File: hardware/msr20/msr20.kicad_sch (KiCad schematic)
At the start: 0 parts

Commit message: add cd74hc4046 symbol
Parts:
- added C1: 200n, symbol Device:C
- added C2: 2.2u, symbol Device:C
- added C3: 1.5p, symbol Device:C
- added L1: 5.1n, symbol Device:L
- added L2: 15u, symbol Device:L
- added R1: 1.5k, symbol Device:R
- added U1: RF-BPF, symbol msr20:RF-BPF
- added U2: BGA616, symbol msr20:BGA616
- added U3: ADE-1+, symbol msr20:ADE-1+
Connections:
- new net: C2.1, L1.2, R1.2, U2.3 (OUT)
- new net: C2.2, U3.3 (RF)
- new net: C1.1, L2.2, U2.1 (IN)
- new net: C1.2, R1.1
- new net: C3.1, L2.1, U1.7 (OUT), U1.8 (OUT)
- new net +3.3V: L1.1
- new net GND: C3.2, U1.3 (GND), U1.4 (GND), U1.5 (GND), U1.6 (GND), U2.2 (GND), U2.4 (GND), U3.1 (GND), U3.4 (GND), U3.5 (GND)
- new net RF-IN: U1.1 (IN), U1.2 (IN)

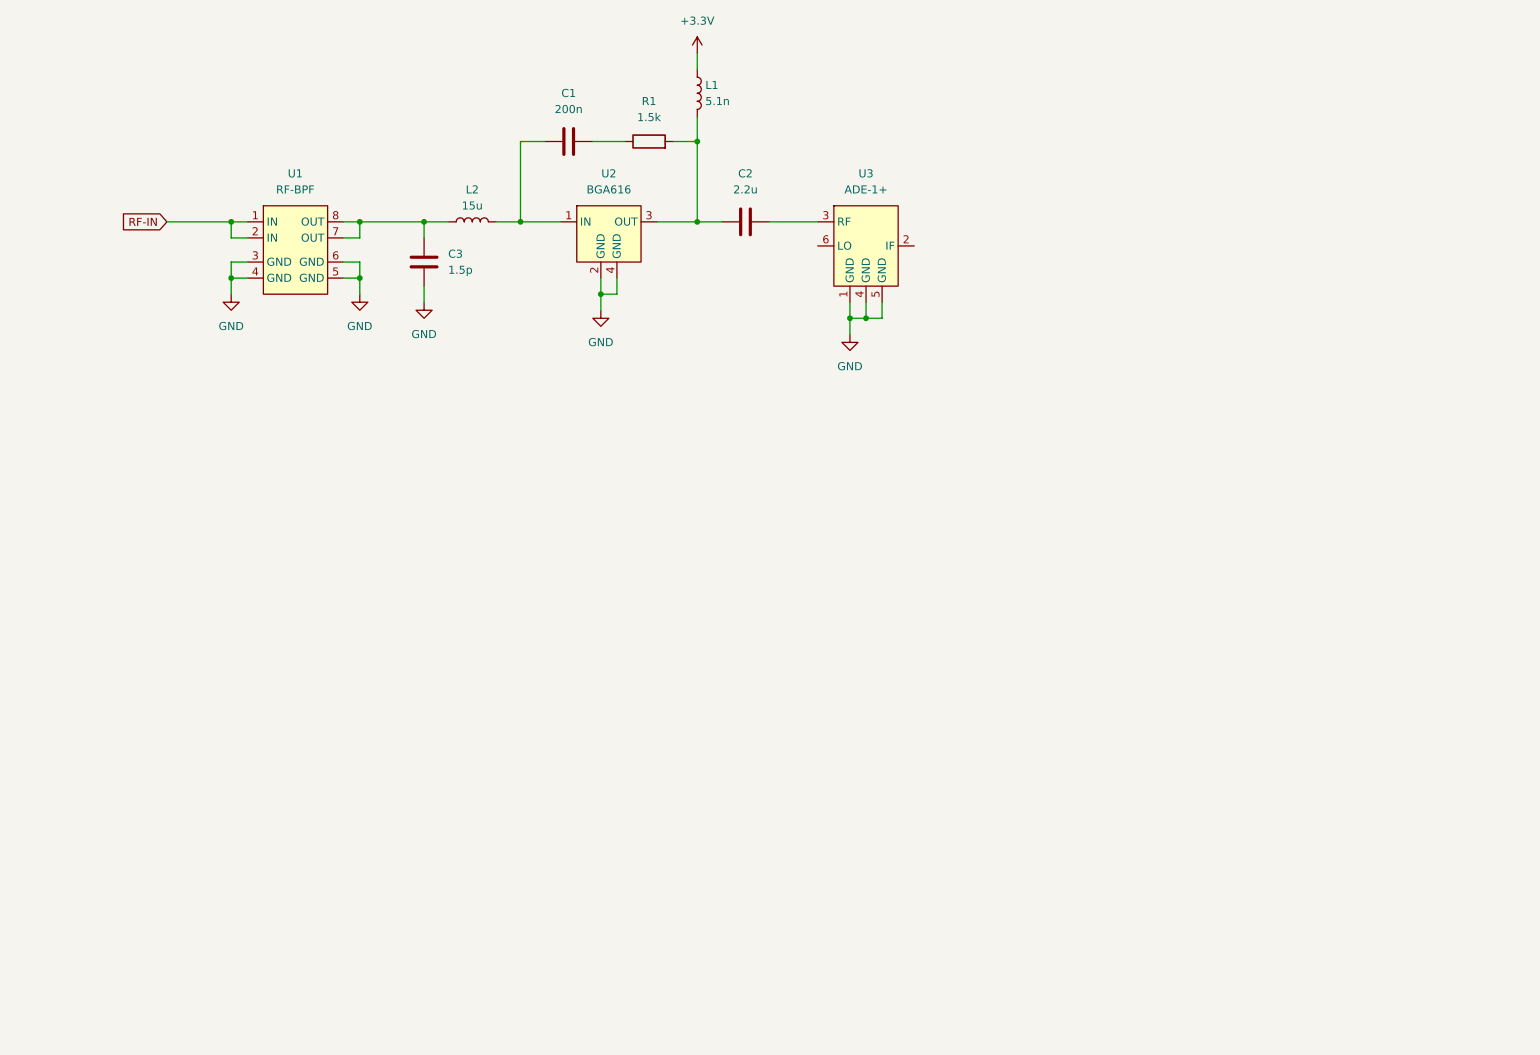
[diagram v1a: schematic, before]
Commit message: add adc and pico to sch
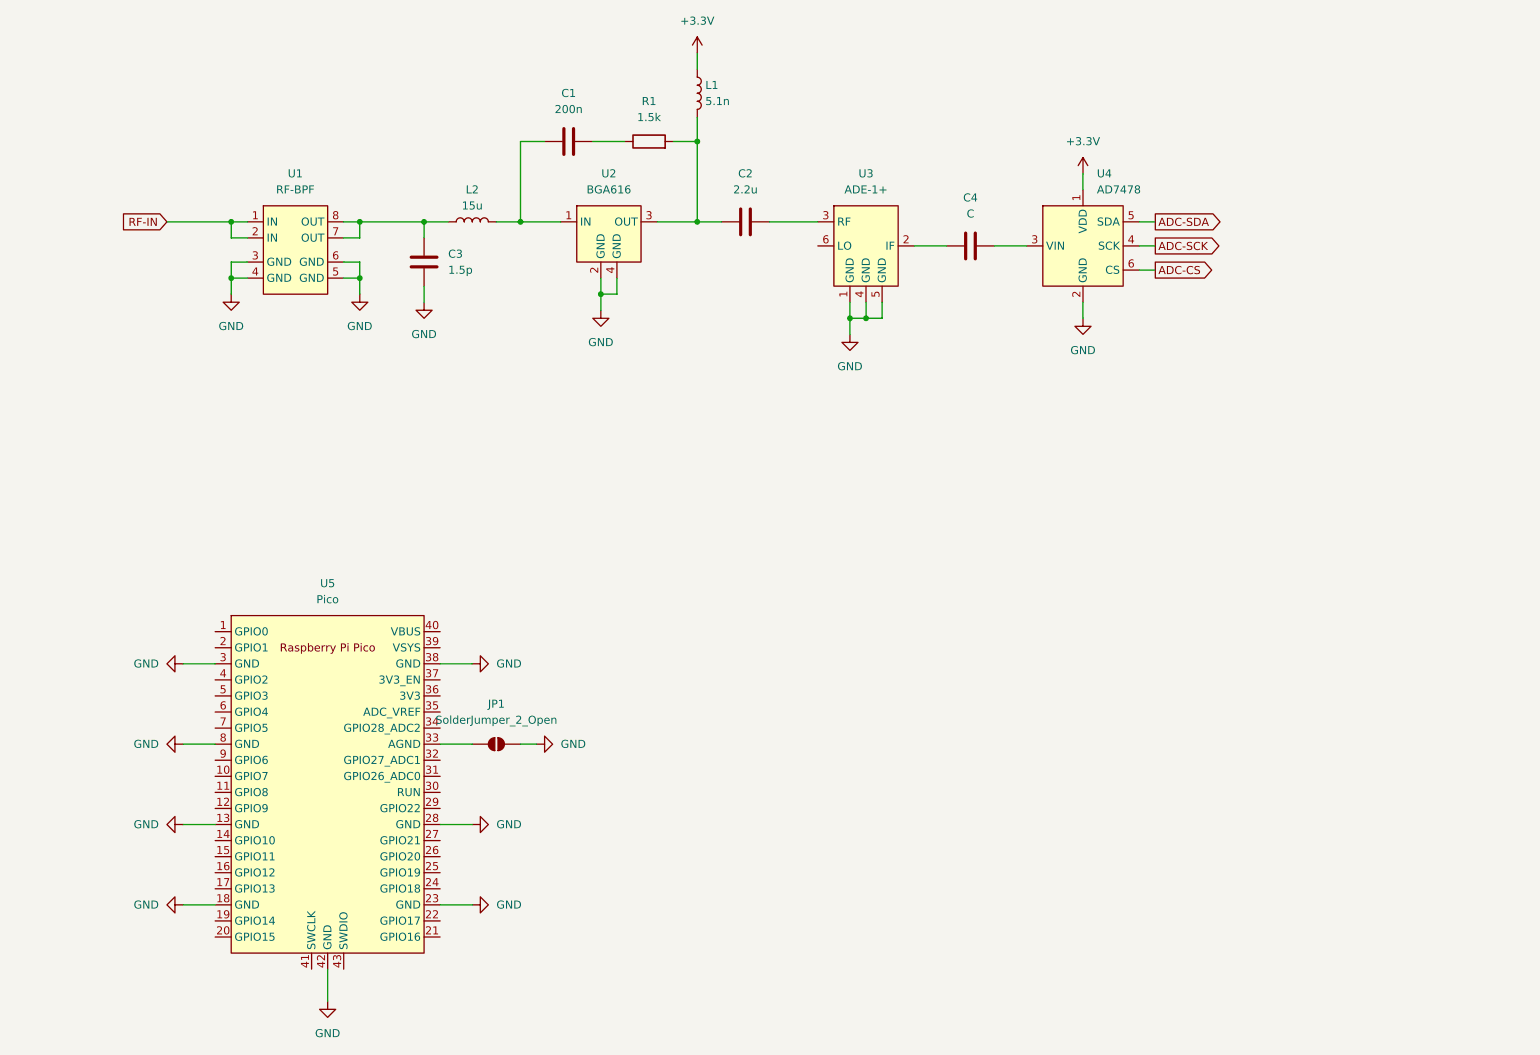
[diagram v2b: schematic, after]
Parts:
- added C4: C, symbol Device:C
- added JP1: SolderJumper_2_Open, symbol Jumper:SolderJumper_2_Open
- added U4: AD7478, symbol msr20:AD7478
- added U5: Pico, RPi_Pico:RPi_Pico_SMD_TH, symbol MCU_RaspberryPi_and_Boards:Pico
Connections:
- net +3.3V: now also U4.1 (VDD)
- net GND: now also JP1.2 (B), U4.2 (GND), U5.13 (GND), U5.18 (GND), U5.23 (GND), U5.28 (GND), U5.3 (GND), U5.38 (GND), U5.42 (GND), U5.8 (GND)
- net at U3.2 (IF): now also C4.1
- new net: JP1.1 (A), U5.33 (AGND)
- new net: C4.2, U4.3 (VIN)
- new net ADC-CS: U4.6 (CS)
- new net ADC-SCK: U4.4 (SCK)
- new net ADC-SDA: U4.5 (SDA)

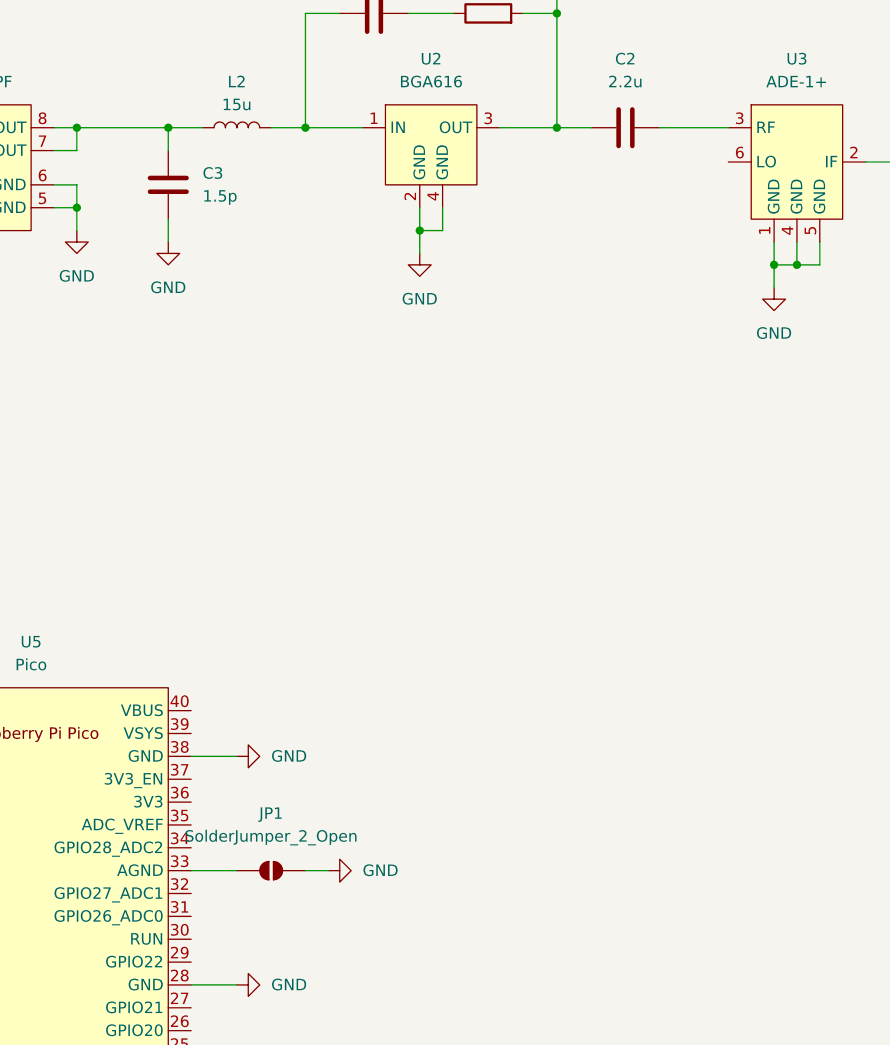
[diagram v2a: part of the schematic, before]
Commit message: Add pll schematic
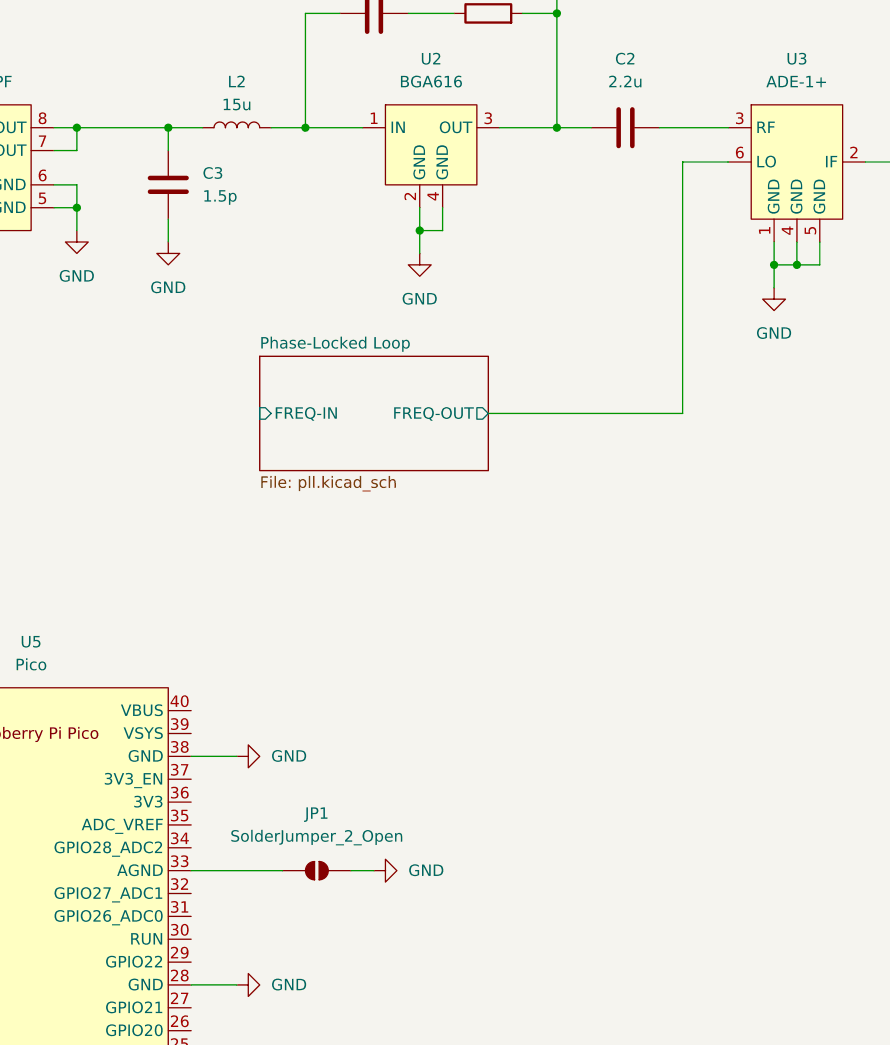
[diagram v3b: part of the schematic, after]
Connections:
- net Phase-Locked Loop/FREQ-OUT: now reaches U3.6 (LO)
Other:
- added sheet Phase-Locked Loop (pll.kicad_sch)
- moved on the sheet: JP1
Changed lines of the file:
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@@
+	(wire
+		(pts
+			(xy 148.59 67.31) (xy 153.67 67.31)
+		)
+		(stroke
+			(width 0)
+			(type default)
+		)
+	)
 	(wire
 		(pts
@@
 	(wire
 		(pts
+			(xy 148.59 95.25) (xy 148.59 67.31)
+		)
+		(stroke
+			(width 0)
+			(type default)
+		)
+	)
+	(wire
+		(pts
 			(xy 204.47 71.12) (xy 207.01 71.12)
 		)
@@
 	(wire
 		(pts
+			(xy 127 95.25) (xy 148.59 95.25)
+		)
+		(stroke
+			(width 0)
+			(type default)
+		)
+	)
+	(wire
+		(pts
 			(xy 119.38 74.93) (xy 119.38 77.47)
 		)
@@
 	(wire
 		(pts
-			(xy 106.68 146.05) (xy 109.22 146.05)
+			(xy 111.76 146.05) (xy 114.3 146.05)
 		)
 		(stroke
@@
 	(wire
 		(pts
-			(xy 93.98 146.05) (xy 99.06 146.05)
+			(xy 93.98 146.05) (xy 104.14 146.05)
 		)
 		(stroke
@@
 	(symbol
 		(lib_id "power:GND")
-		(at 109.22 146.05 90)
+		(at 114.3 146.05 90)
 		(unit 1)
 		(exclude_from_sim no)
@@
 		(fields_autoplaced yes)
 		(property "Reference" "#PWR018"
-			(at 115.57 146.05 0)
+			(at 120.65 146.05 0)
 			(effects
 				(font
@@
 		)
 		(property "Value" "GND"
-			(at 113.03 146.0499 90)
+			(at 118.11 146.0499 90)
 			(effects
 				(font
@@
 		)
 		(property "Footprint" ""
-			(at 109.22 146.05 0)
+			(at 114.3 146.05 0)
 			(effects
 				(font
@@
 		)
 		(property "Datasheet" ""
-			(at 109.22 146.05 0)
+			(at 114.3 146.05 0)
 			(effects
 				(font
@@
 		)
 		(property "Description" "Power symbol creates a global label with name \"GND\" , ground"
-			(at 109.22 146.05 0)
+			(at 114.3 146.05 0)
 			(effects
 				(font
@@
 	(symbol
 		(lib_id "Jumper:SolderJumper_2_Open")
-		(at 102.87 146.05 0)
+		(at 107.95 146.05 0)
 		(unit 1)
 		(exclude_from_sim yes)
@@
 		(fields_autoplaced yes)
 		(property "Reference" "JP1"
-			(at 102.87 139.7 0)
+			(at 107.95 139.7 0)
 			(effects
 				(font
@@
 		)
 		(property "Value" "SolderJumper_2_Open"
-			(at 102.87 142.24 0)
-			(effects
-				(font
-					(size 1.27 1.27)
-				)
-			)
-		)
-		(property "Footprint" ""
-			(at 102.87 146.05 0)
+			(at 107.95 142.24 0)
+			(effects
+				(font
+					(size 1.27 1.27)
+				)
+			)
+		)
+		(property "Footprint" ""
+			(at 107.95 146.05 0)
 			(effects
 				(font
@@
 		)
 		(property "Datasheet" "~"
-			(at 102.87 146.05 0)
+			(at 107.95 146.05 0)
 			(effects
 				(font
@@
 		)
 		(property "Description" "Solder Jumper, 2-pole, open"
-			(at 102.87 146.05 0)
+			(at 107.95 146.05 0)
 			(effects
 				(font
@@
 				)
 			)
+		)
+	)
+	(sheet
+		(at 101.6 88.9)
+		(size 25.4 12.7)
+		(fields_autoplaced yes)
+		(stroke
+			(width 0.1524)
+			(type solid)
+		)
+		(fill
+			(color 0 0 0 0.0000)
+		)
+		(property "Sheetname" "Phase-Locked Loop"
+			(at 101.6 88.1884 0)
+			(effects
+				(font
+					(size 1.27 1.27)
+				)
+				(justify left bottom)
+			)
+		)
+		(property "Sheetfile" "pll.kicad_sch"
+			(at 101.6 102.1846 0)
+			(effects
+				(font
+					(size 1.27 1.27)
+				)
+				(justify left top)
+			)
+		)
+		(pin "FREQ-IN" input
+			(at 101.6 95.25 180)
+			(effects
+				(font
+					(size 1.27 1.27)
+				)
+				(justify left)
+			)
+		)
+		(pin "FREQ-OUT" output
+			(at 127 95.25 0)
+			(effects
+				(font
+					(size 1.27 1.27)
+				)
+				(justify right)
+			)
+		)
+		(instances
+			(project "msr20"
+				(path "/827e4c90-6b76-4aba-b6da-8b66ea005818"
+					(page "2")
+				)
+			)

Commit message: save
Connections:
- net ADC-CS: now also U5.25 (GPIO19)
- net ADC-SCK: now also U5.24 (GPIO18)
- net ADC-SDA: now also U5.21 (GPIO16)
- no-connect marks 0 -> 1
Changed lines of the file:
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@@
 		(color 0 0 0 0)
 	)
+	(no_connect
+		(at 93.98 173.99)
+	)
 	(wire
 		(pts
@@
 	(wire
 		(pts
+			(xy 93.98 176.53) (xy 99.06 176.53)
+		)
+		(stroke
+			(width 0)
+			(type default)
+		)
+	)
+	(wire
+		(pts
 			(xy 60.96 72.39) (xy 60.96 74.93)
 		)
@@
 	(wire
 		(pts
+			(xy 93.98 166.37) (xy 99.06 166.37)
+		)
+		(stroke
+			(width 0)
+			(type default)
+		)
+	)
+	(wire
+		(pts
 			(xy 204.47 71.12) (xy 207.01 71.12)
 		)
@@
 		(pts
 			(xy 195.58 55.88) (xy 195.58 58.42)
+		)
+		(stroke
+			(width 0)
+			(type default)
+		)
+	)
+	(wire
+		(pts
+			(xy 93.98 168.91) (xy 99.06 168.91)
 		)
 		(stroke
@@
 		)
 	)
+	(global_label "ADC-SDA"
+		(shape input)
+		(at 99.06 176.53 0)
+		(fields_autoplaced yes)
+		(effects
+			(font
+				(size 1.27 1.27)
+			)
+			(justify left)
+		)
+		(property "Intersheetrefs" "${INTERSHEET_REFS}"
+			(at 110.8143 176.53 0)
+			(effects
+				(font
+					(size 1.27 1.27)
+				)
+				(justify left)
+				(hide yes)
+			)
+		)
+	)
 	(global_label "RF-IN"
 		(shape input)
@@
 	)
 	(global_label "ADC-CS"
+		(shape input)
+		(at 99.06 166.37 0)
+		(fields_autoplaced yes)
+		(effects
+			(font
+				(size 1.27 1.27)
+			)
+			(justify left)
+		)
+		(property "Intersheetrefs" "${INTERSHEET_REFS}"
+			(at 109.7257 166.37 0)
+			(effects
+				(font
+					(size 1.27 1.27)
+				)
+				(justify left)
+				(hide yes)
+			)
+		)
+	)
+	(global_label "ADC-CS"
 		(shape output)
 		(at 207.01 71.12 0)
@@
 			(effects
 				(font
+					(size 1.27 1.27)
+				)
+				(justify left)
+				(hide yes)
+			)
+		)
+	)
+	(global_label "ADC-SCK"
+		(shape input)
+		(at 99.06 168.91 0)
+		(fields_autoplaced yes)
+		(effects
+			(font
+				(size 1.27 1.27)
+			)
+			(justify left)
+		)
+		(property "Intersheetrefs" "${INTERSHEET_REFS}"
+			(at 110.9957 168.91 0)
+			(effects
+				(font

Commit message: assign footprints for active components
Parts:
- U1: footprint (none) -> msr20:RF-BPF
- U2: footprint (none) -> msr20:BGA616
- U3: footprint (none) -> msr20:ADE-1+
- U4: footprint (none) -> Package_TO_SOT_SMD:SOT-23-6
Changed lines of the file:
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@@
 			)
 		)
-		(property "Footprint" ""
+		(property "Footprint" "msr20:BGA616"
 			(at 120.65 60.96 0)
 			(effects
@@
 			)
 		)
-		(property "Footprint" ""
+		(property "Footprint" "msr20:RF-BPF"
 			(at 71.12 60.96 0)
 			(effects
@@
 			)
 		)
-		(property "Footprint" ""
+		(property "Footprint" "msr20:ADE-1+"
 			(at 161.29 60.96 0)
 			(effects
@@
 			)
 		)
-		(property "Footprint" ""
+		(property "Footprint" "Package_TO_SOT_SMD:SOT-23-6"
 			(at 195.58 60.96 0)
 			(effects

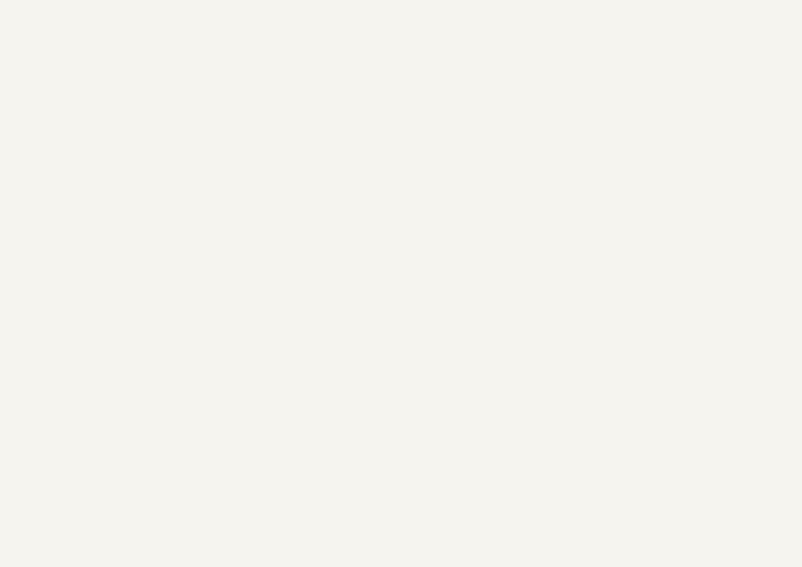
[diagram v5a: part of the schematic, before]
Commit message: add power sheet to schematic, add 3.3v, 5v regulators to schematic
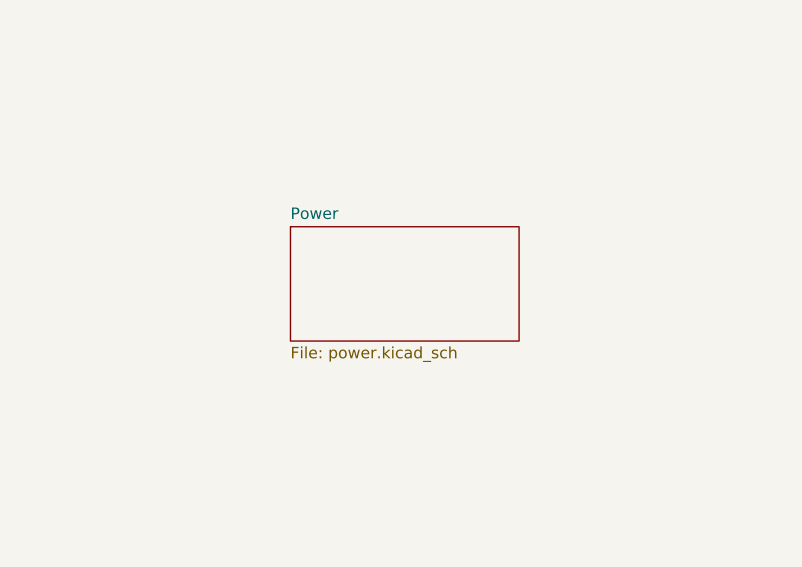
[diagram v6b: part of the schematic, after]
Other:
- added sheet Power (power.kicad_sch)
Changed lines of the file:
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@@
+		)
+	)
+	(sheet
+		(at 165.1 127)
+		(size 25.4 12.7)
+		(fields_autoplaced yes)
+		(stroke
+			(width 0.1524)
+			(type solid)
+		)
+		(fill
+			(color 0 0 0 0.0000)
+		)
+		(property "Sheetname" "Power"
+			(at 165.1 126.2884 0)
+			(effects
+				(font
+					(size 1.27 1.27)
+				)
+				(justify left bottom)
+			)
+		)
+		(property "Sheetfile" "power.kicad_sch"
+			(at 165.1 140.2846 0)
+			(effects
+				(font
+					(size 1.27 1.27)
+				)
+				(justify left top)
+			)
+		)
+		(instances
+			(project "msr20"
+				(path "/827e4c90-6b76-4aba-b6da-8b66ea005818"
+					(page "3")
+				)
+			)
 		)
 	)
